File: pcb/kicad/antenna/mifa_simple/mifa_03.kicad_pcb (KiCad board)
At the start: 2 copper layers, 19 x 32 mm, 1 part

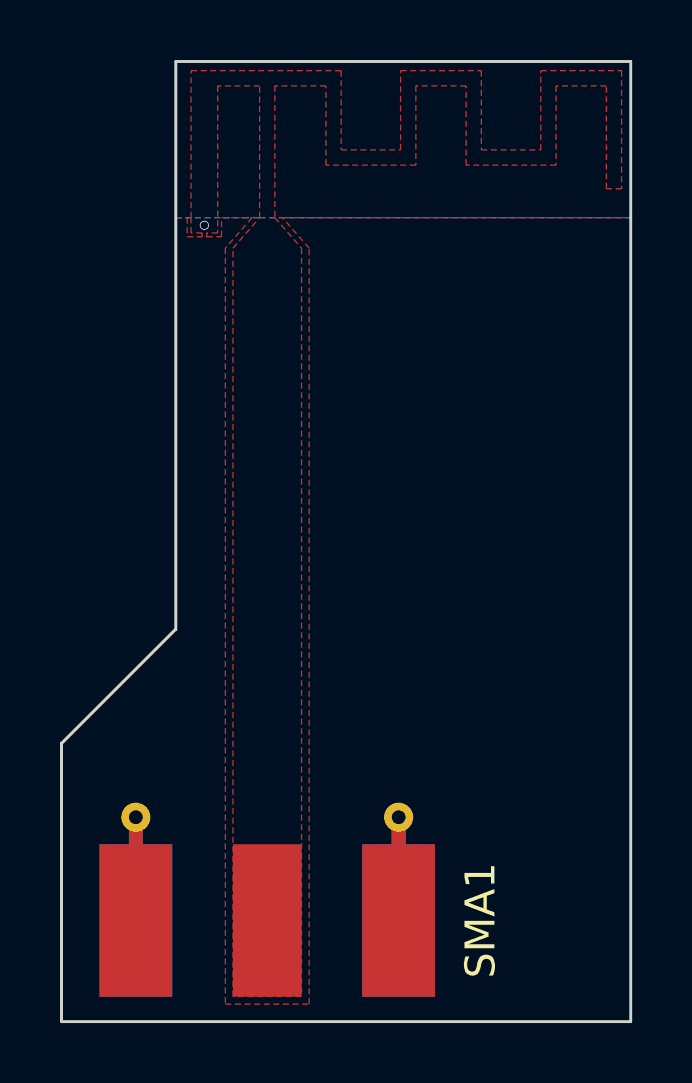
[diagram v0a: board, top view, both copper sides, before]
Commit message: Add final tiling for first revision test board
Tiled the remainder of the MIFA antennas as well as two antennas for
potential chip antennas.
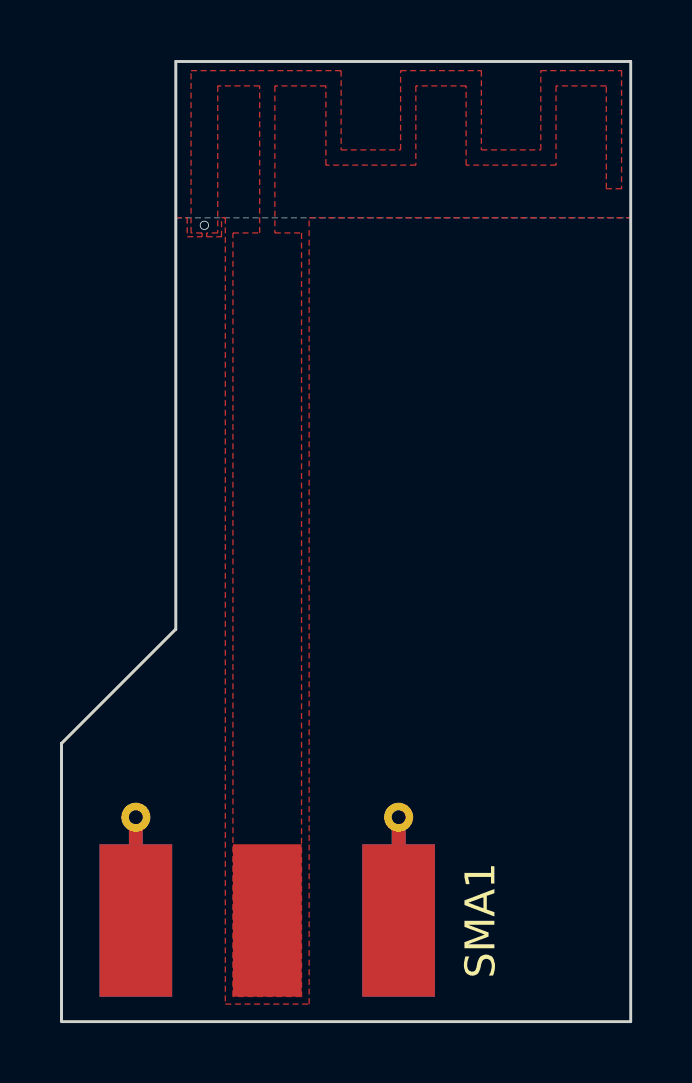
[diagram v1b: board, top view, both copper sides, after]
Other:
- rule via_min_drill: 0.2032 -> 0.254
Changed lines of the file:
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@@
     (via_drill 0.4)
     (via_min_size 0.254)
-    (via_min_drill 0.2032)
+    (via_min_drill 0.254)
     (user_via 0.3048 0.254)
     (user_via 0.381 0.3048)
@@
     (aux_axis_origin 144.018 126.5047)
     (grid_origin 144.018 126.5047)
-    (visible_elements 7FFFFFDF)
+    (visible_elements 7FFFFFFF)
     (pcbplotparams
       (layerselection 0x030f0_80000001)
@@
       (drillshape 0)
       (scaleselection 1)
-      (outputdirectory ""))
+      (outputdirectory mifa_03_art/))
   )
   (net 0 "")
@@
       (net 1 GND))
   )
+  (gr_line (start 147.828 113.4237) (end 147.828 94.5007) (angle 90) (layer Edge.Cuts) (width 0.1))
   (gr_line (start 162.9918 94.5007) (end 147.828 94.5007) (angle 90) (layer Edge.Cuts) (width 0.09652))
   (gr_line (start 162.9918 126.5047) (end 162.9918 94.5007) (angle 90) (layer Edge.Cuts) (width 0.09652))
   (gr_line (start 144.018 126.5047) (end 162.9918 126.5047) (angle 90) (layer Edge.Cuts) (width 0.09652))
-  (gr_line (start 147.828 113.4237) (end 147.828 94.5007) (angle 90) (layer Edge.Cuts) (width 0.1))
   (gr_line (start 144.018 117.2337) (end 147.828 113.4237) (angle 90) (layer Edge.Cuts) (width 0.1))
   (gr_line (start 144.018 126.5047) (end 144.018 117.2337) (angle 90) (layer Edge.Cuts) (width 0.1))
@@
         (xy 162.179 95.3135) (xy 160.5026 95.3135) (xy 160.5026 97.9551) (xy 157.5054 97.9551) (xy 157.5054 95.3135)
         (xy 155.829 95.3135) (xy 155.829 97.9551) (xy 152.8318 97.9551) (xy 152.8318 95.3135) (xy 151.13 95.3135)
-        (xy 151.13 99.7077) (xy 152.019 100.7237) (xy 152.019 125.6665) (xy 149.733 125.6665) (xy 149.733 100.7237)
-        (xy 150.622 99.7077) (xy 150.622 95.3135) (xy 149.225 95.3135) (xy 149.225 100.2157) (xy 148.8567 100.2157)
-        (xy 148.8567 100.3427) (xy 149.352 100.3427) (xy 149.352 99.7077) (xy 150.368 99.7077) (xy 149.479 100.7237)
-        (xy 149.479 125.9205) (xy 152.273 125.9205) (xy 152.273 100.7237) (xy 151.384 99.7077) (xy 162.9918 99.7077)
-        (xy 162.9918 126.5047) (xy 144.018 126.5047) (xy 144.018 117.2337) (xy 147.828 113.4237) (xy 147.828 99.7077)
-        (xy 148.209 99.7077) (xy 148.209 100.3427) (xy 148.7043 100.3427) (xy 148.7043 100.2157) (xy 148.336 100.2157)
-        (xy 148.336 99.7077) (xy 148.336 94.8055) (xy 153.3398 94.8055)
+        (xy 151.13 100.2157) (xy 152.019 100.2157) (xy 152.019 125.6665) (xy 149.733 125.6665) (xy 149.733 100.2157)
+        (xy 150.622 100.2157) (xy 150.622 95.3135) (xy 149.225 95.3135) (xy 149.225 100.2157) (xy 148.8567 100.2157)
+        (xy 148.8567 100.3427) (xy 149.352 100.3427) (xy 149.352 99.7077) (xy 149.479 99.7077) (xy 149.479 125.9205)
+        (xy 152.273 125.9205) (xy 152.273 99.7077) (xy 162.9918 99.7077) (xy 162.9918 126.5047) (xy 144.018 126.5047)
+        (xy 144.018 117.2337) (xy 147.828 113.4237) (xy 147.828 99.7077) (xy 148.209 99.7077) (xy 148.209 100.3427)
+        (xy 148.7043 100.3427) (xy 148.7043 100.2157) (xy 148.336 100.2157) (xy 148.336 94.8055) (xy 153.3398 94.8055)
       )
     )
@@
     (polygon
       (pts
-        (xy 162.9918 99.7077) (xy 162.9918 126.5047) (xy 144.018 126.5047) (xy 144.018 117.2337) (xy 147.828 113.4237)
-        (xy 147.828 99.7077) (xy 150.622 99.7077)
+        (xy 162.9918 126.5047) (xy 144.018 126.5047) (xy 144.018 117.2337) (xy 147.828 113.4237) (xy 147.828 99.7077)
+        (xy 162.9918 99.7077)
       )
     )
